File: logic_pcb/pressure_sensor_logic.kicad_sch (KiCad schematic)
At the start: 24 parts, among them J11 TYPE-C-31-M-12, J2 Conn_01x02_Pin, J3 Conn_01x04_Pin, J4 Conn_01x02_Pin, J5 Conn_01x02_Pin, J6 Conn_01x02_Pin, SW2 SW_Push, U3 AP2112K-3.3, U4 STM32G030F6Px, U5 CH340E

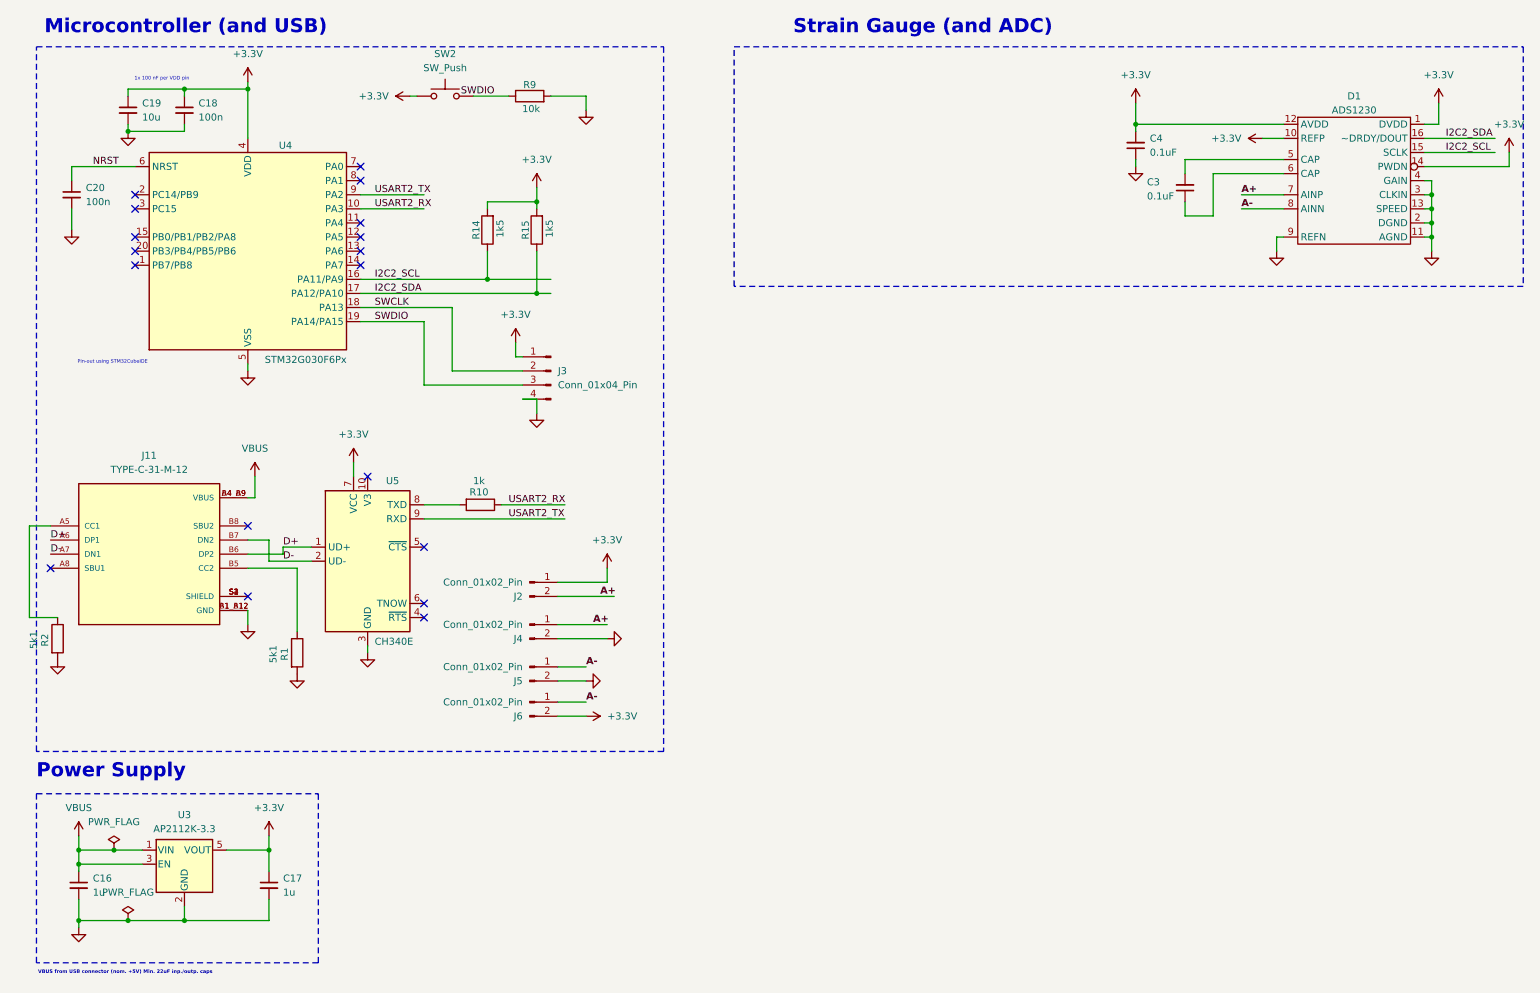
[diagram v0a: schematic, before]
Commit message: mounting_holes_added
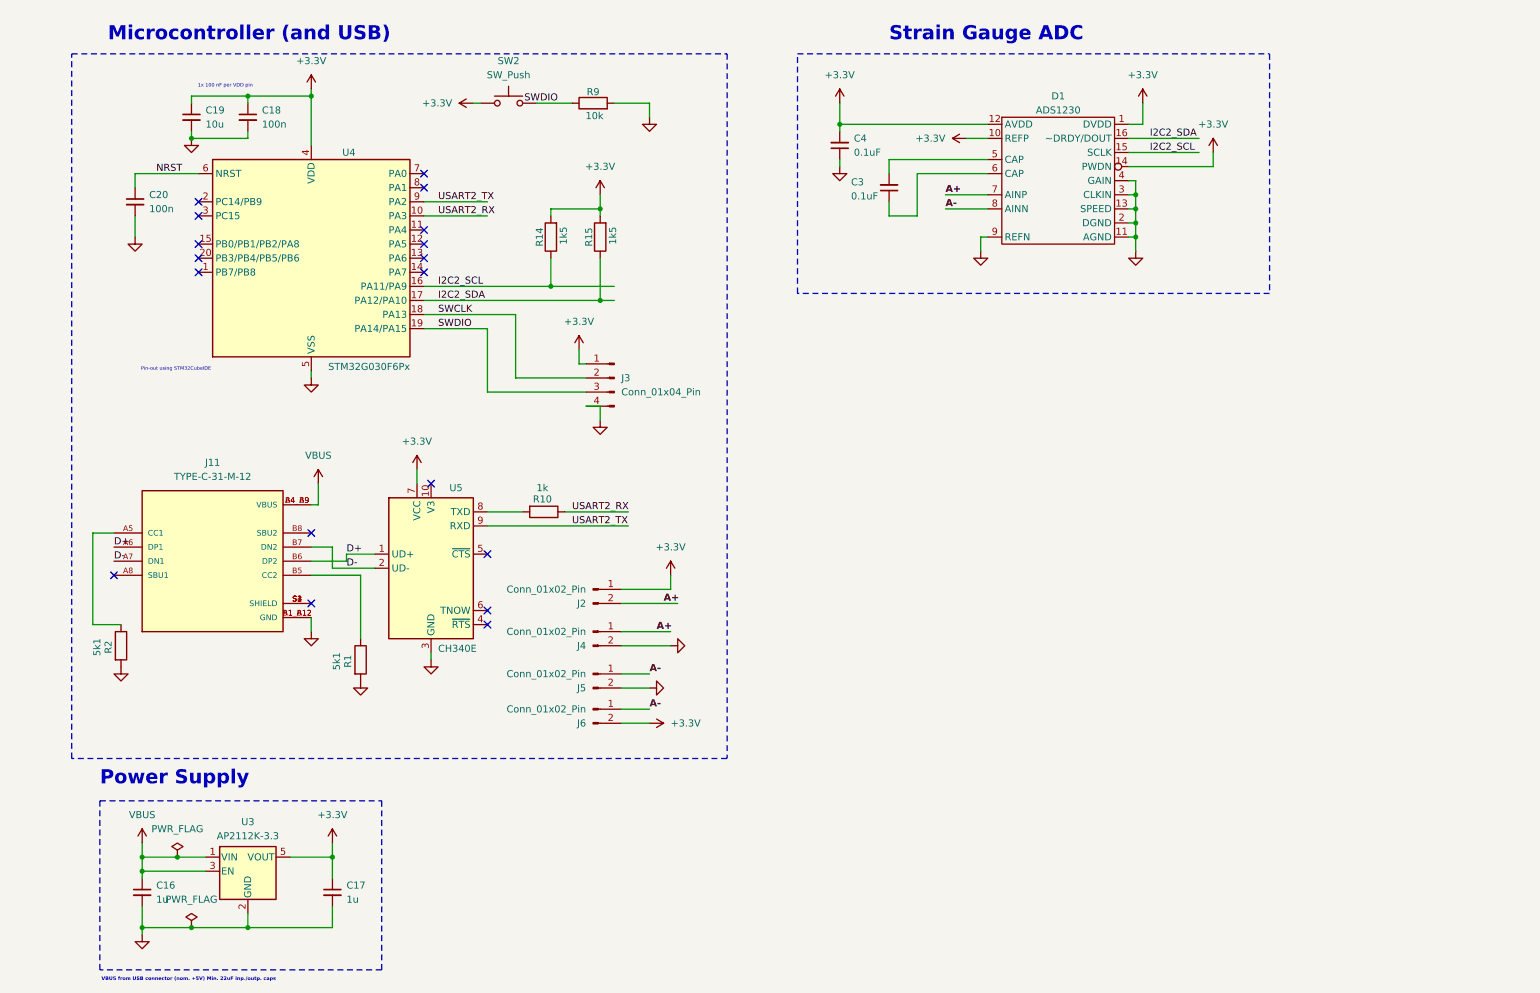
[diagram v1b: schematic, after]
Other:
- note added: "Strain Gauge ADC"
- note removed: "Strain Gauge (and ADC)"
- moved on the sheet: C16, C17, C18, C19, C20, C3, C4, D1, J11, J2, J3, J4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
